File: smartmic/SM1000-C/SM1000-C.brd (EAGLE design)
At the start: 65 x 90 mm, 185 parts, among them CN1 HDR100-3, CN10 MJ-3523-SMT, CN11 HDR100-3, CN12 HRS-DF11-16DS, CN2 MOLEX-MINI-B-SMT, CN3 RASM722PX, CN4 RJ-45, CN5 MJ-3523-SMT, CN6 SJ-3524-SMT, CN7 MJ-3523-SMT, CN8 SJ-3524-SMT, CN9 MJ-3523-SMT, J1 JMP-2PIN, J3 JMP-2PIN, J4 JMP-2PIN, P1 TPAD50, P10 TPAD50, P11 TPAD50, P12 TPAD50, P13 TPAD50, P14 TPAD50, P15 TPAD50, P16 TPAD50, P17 TPAD50, P18 TPAD50, P19 TPAD50, P2 TPAD50, P20 TPAD50, P3 TPAD50, P4 TPAD50, P5 TPAD50, P6 TPAD50, P7 TPAD50, P8 TPAD50, P9 TPAD50, SW1 SW-BOURNS-7914S, SW2 SW-BOURNS-7914S, SW3 DPDT, SW4 SW-BOURNS-7914S, SW5 SW-BOURNS-7914J, T1 SM-LP-5001, T2 SM-LP-5001, U1 STM32F405, U2 LD3985M33R, U3 STMPS2141, U4 EMIF02-USB03F2, U5 TPS54329E, U6 LMV341, U7 LMV341, U8 LM386M-1, U9 LMV341

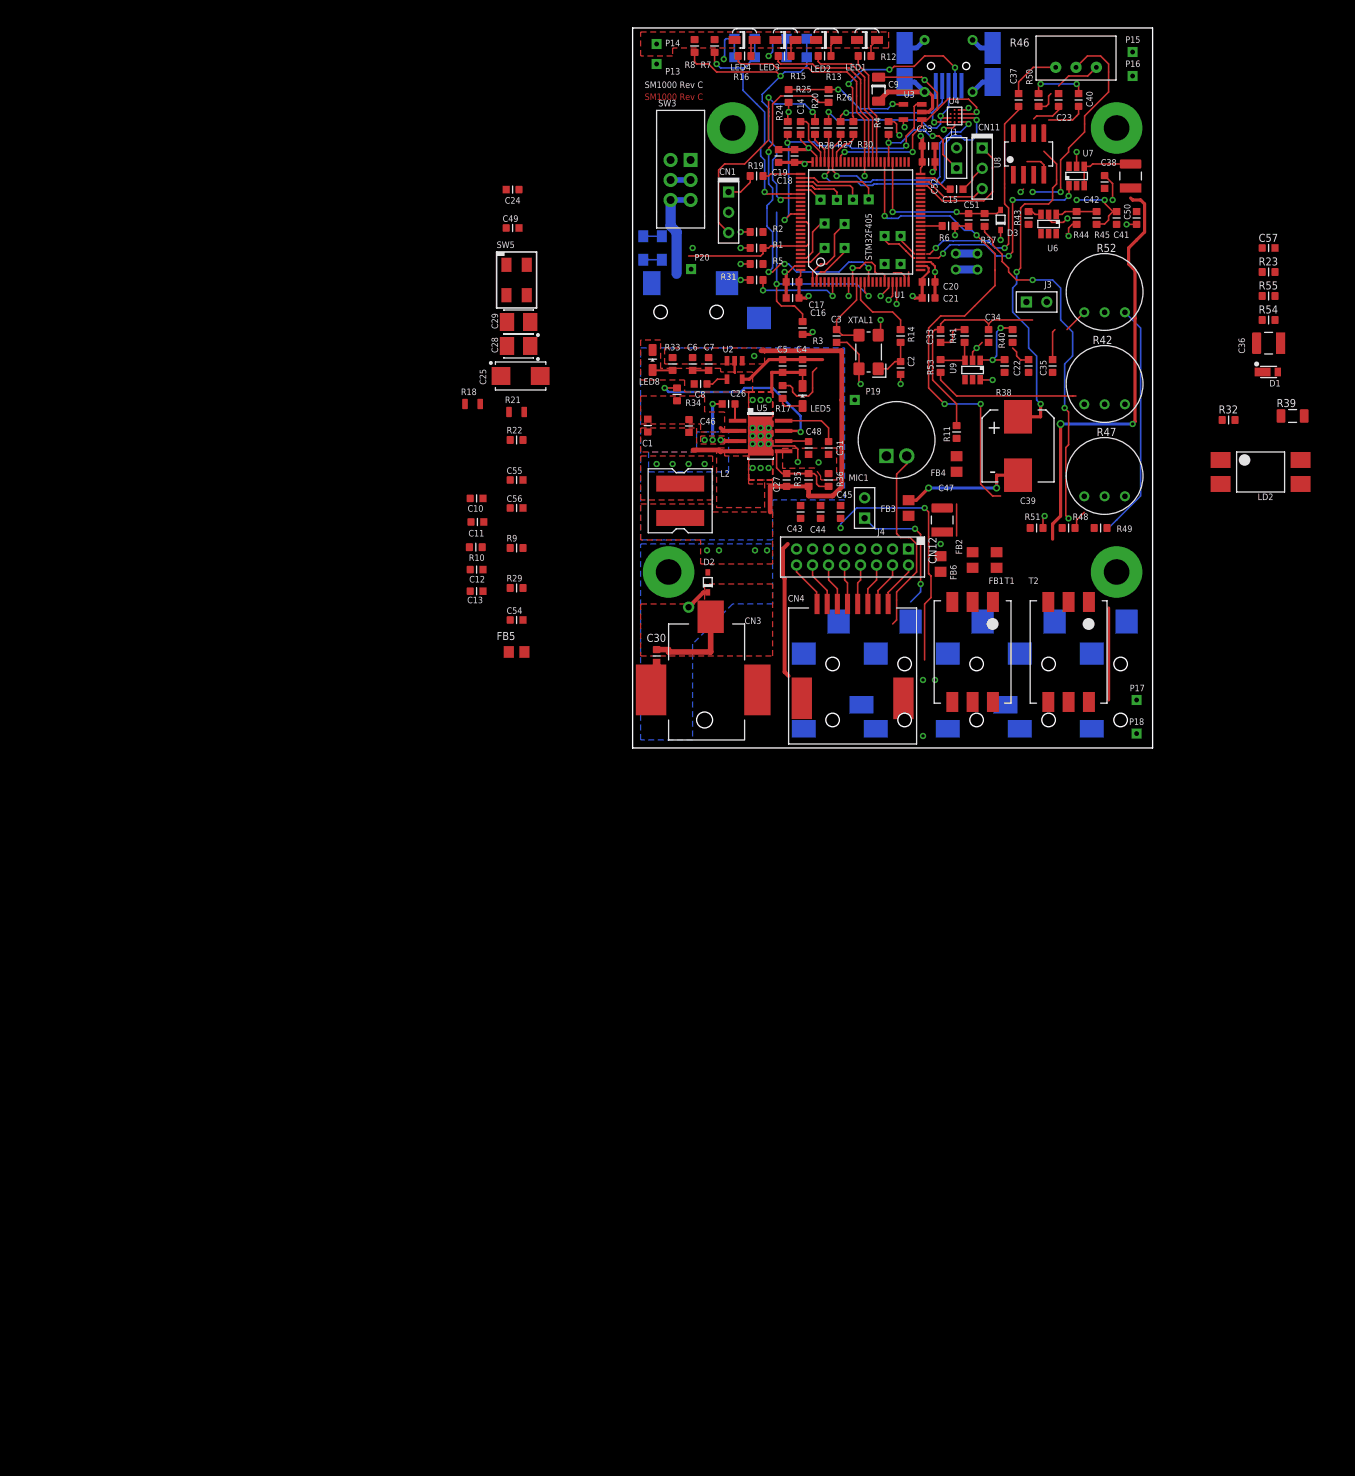
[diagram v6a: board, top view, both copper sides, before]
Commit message: Recovery from Eagle ERC problem RGB
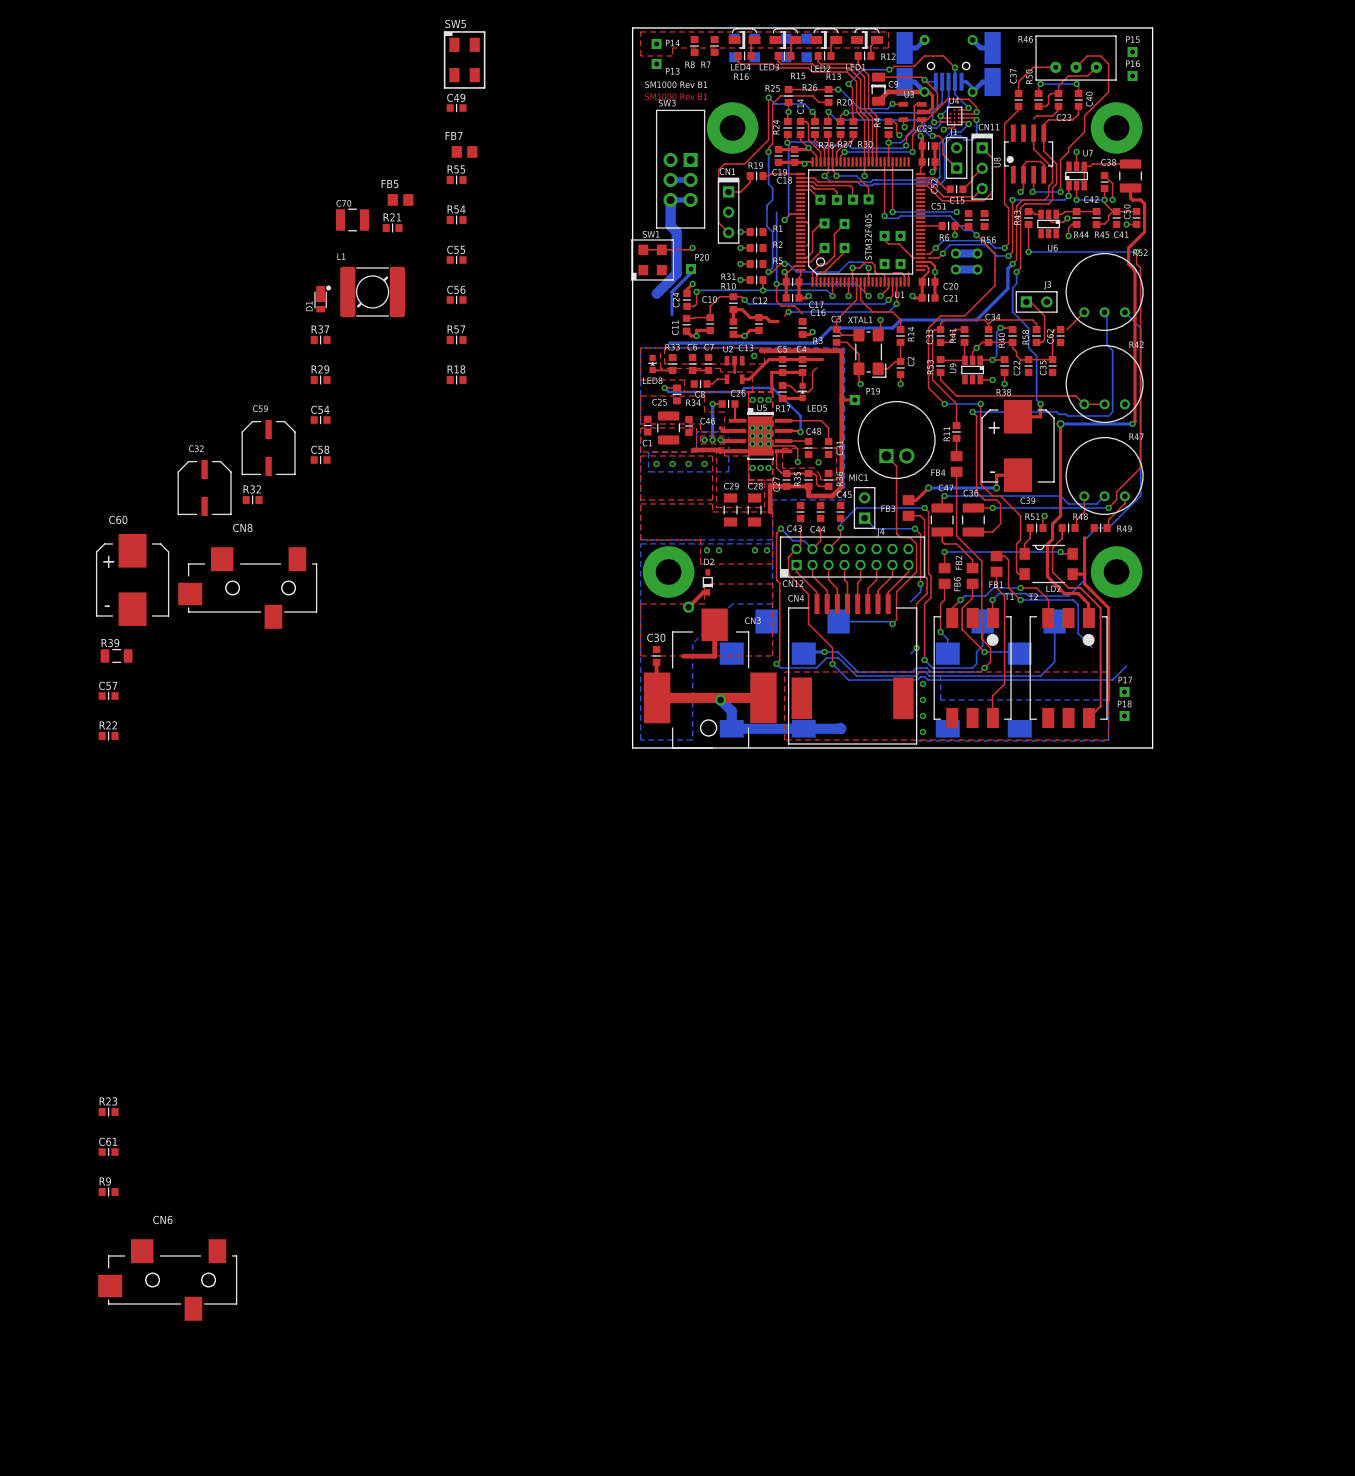
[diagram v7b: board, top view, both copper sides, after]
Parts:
- removed D3: BAT60J, _RoweTel:SOD323R_INFINEON
- removed L2: 4.7uH, _RoweTel:SRN6045
- added C32, C59: 100uF,6.3V,EL, _RoweTel:NICHICON-WX-6.3
- added C58, C61, C62: 100nF,16V, AA-ipc-7351-capacitor:CAPC1608X92N
- added C60: 220uF,25V, _RoweTel:CAP-CHEMI-HA0
- added C70: 22uF,25V,1210, ipc-7351-capacitor:CAPC3225X168N
- added FB7: FB0805, _RoweTel:FE0805
- added L1: 4.2uH, _RoweTel:SRR5028
- added R56, R58: 2.2K,1%, AA-ipc-7351-resistor:RESC1608X55N
- added R57: 470,1%, AA-ipc-7351-resistor:RESC1608X55N
- C25: value 22uF,25V,3528,Tant -> 22uF,25V,1210; device AA-ipc-7351-capacitor:CAPMP6032X280N -> ipc-7351-capacitor:CAPC3225X168N
- C28, C29: value 10uF,25V,3528,Tant -> 10uF,25V,1206; device AA-ipc-7351-capacitor:CAPMP3528X210N -> ipc-7351-capacitor:CAPC3215X168N
- C40: value 47nF,25V -> 100nF,25V
- C54: value 1nF,16V -> 1nF,25V
- CN12: value HRS-DF11-16DS -> DF11-16DS
- CN3: device _RoweTel:RASM722PX -> _RoweTel:RASM712PX
- CN6, CN8: value SJ-3524-SMT -> SJ-3524
- FB5: value (none) -> FB0805
- LD2: device _RoweTel:LTV-817S -> _RoweTel:SMD4
- R18, R21: device _RoweTel:RR0805 -> AA-ipc-7351-resistor:RESC1608X55N
- R32: value (none) -> 100,1%
- R37: value 2.2K,1% -> 10K,1%
- SW1: device SM1000:SW-BOURNS-7914S -> SM1000-2L-70x90:SW-BOURNS-7914S
- moved R23 179.0 mm to (-65.5, -45.5)
- moved C57 155.4 mm to (-65.5, 6.50)
- moved R39 150.0 mm to (-64.5, 11.5)
- moved CN6 123.7 mm to (-56.5, -66.5), flipped to the top, turned to 0 degrees
- moved R32 122.4 mm to (-47.5, 31.0)
- moved D1 119.3 mm to (-39.0, 55.5), turned to 0 degrees
- moved R55 102.5 mm to (-22.0, 71.0)
- moved R54 102.3 mm to (-22.0, 66.0)
- moved R9 95.3 mm to (-65.5, -55.5)
- moved R37 84.3 mm to (-39.0, 51.0), turned to 0 degrees
- moved CN8 72.7 mm to (-46.5, 20.0), flipped to the top, turned to 0 degrees
- moved R22 63.0 mm to (-65.5, 1.50)
- moved FB5 58.3 mm to (-29.0, 68.5)
- moved CN10 47.2 mm to (16.0, 8.00), turned to 270 degrees
- moved C12 46.8 mm to (15.8, 53.0), turned to 270 degrees
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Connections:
- net !CPTT! renamed !CPPT!
- net N$15 renamed +VEXT
- removed net BACK: R8.2, SW4.1, SW4.2, U1.82
- removed net BOOT0: R1.2, SW1.1, SW1.2, U1.88, U1.94
- removed net N$32 (its old number): C54.2, R29.1, R42.1, U9.4
- removed net N$37 (its old number): U8.6
- removed net N$85: CN10.2, R37.1
- removed net S$1: T1.3, T2.3
- removed net S$2: R49.1
- removed net SELECT: R7.2, SW2.1, SW2.2, U1.81
- new net !BACK!: R8.1, SW4.3, SW4.4, U1.82
- new net !BOOT0!: R57.1, U1.88, U1.94
- new net !SELECT!: R7.1, SW2.3, SW2.4, U1.81
- new net APTT: CN12.14, CN9.10
- new net MIC: CN12.15, CN7.10
- new net N$11: R55.1, U1.29
- new net N$14: R1.2, R57.2, SW1.1, SW1.2
- new net N$15: C51.1, CN10.2, R37.2, R56.1
- new net N$26: FB4.2, R11.1
- new net N$27: C54.2, R29.2, R42.3, U9.4
- new net N$33: C44.1, FB1.1, T1.6
- new net N$48: C60.1, R39.2, U8.6
- new net N$64: CN6.2, FB1.2
- new net N$72: CN7.2, FB2.2
- new net N$73: CN9.2, FB6.2
- new net N$76: CN5.2, FB4.1
- new net N$78: R48.2, T2.6
- new net N$81: R47.3, R49.2
- new net RF_MIC: C43.2, CN12.11, CN12.12, CN7.1, R49.1, T2.4
- new net RF_PTT: C45.2, CN12.13, CN9.1, LD2.3
- new net RF_SPKR: C44.2, CN12.10, CN12.9, CN6.1, T1.4
- new net SPKR: CN12.16, CN6.4
- net !EXT-PTT!: now also R56.2; no longer C51.1, D3.A, R37.2
- net +5V: now also C28.1, C29.1, L1.2; no longer C28.+, C29.+, L2.2
- net +VIN: now also C25.1, C70.1, R39.1; no longer C25.+
- net AIN2: no longer P4.1, R29.2
- net AVDD: now also U9.6
- net DAC1_OUT: now also R55.2; no longer R55.1
- net DAC2_OUT: now also R22.1, R54.2; no longer R22.2, R54.1
- net GND: now also C25.2, C28.2, C29.2, C32.2, C58.1, C59.2, C60.2, C61.2, C62.2, C70.2, CN10.1, CN3.1, CN3.3, CN4.10, CN4.9, CN5.1, CN8.1, R22.2, SW2.1, SW2.2, SW4.1, SW4.2, T1.3, T2.3; no longer C25.-, C28.-, C29.-, R22.1, R7.1, R8.1
- net N$13: now also R54.1, U1.30; no longer R47.1, R49.2
- net N$24: now also FB5.2
- net N$25: now also R58.1
- net N$29: now also J3.1, R32.2; no longer R55.2, U1.29
- net N$36: now also P4.1, R29.1; no longer R54.2, U1.30
- net N$41: now also R42.1; no longer R42.3
- net N$45: now also C32.1, C62.1, R32.1, R58.2; no longer J3.1
- net N$46: now also C58.2, C59.1
- net N$5: now also FB7.2
- net N$51: now also CN12.8; no longer CN12.16
- net N$52: now also CN12.7; no longer CN12.15
- net N$53: now also CN12.6; no longer CN12.14
- net N$54: now also CN12.5; no longer CN12.13
- net N$55: now also CN12.4; no longer CN12.12
- net N$56: now also CN12.3; no longer CN12.11
- net N$57: now also CN12.2; no longer CN12.10
- net N$58: now also CN12.1; no longer CN12.9
- net N$59: now also C61.1
- net N$60: now also CN5.10
- net N$62: now also CN8.4
- net N$74: now also C45.1
- net N$75: now also CN8.2, CN8.3
- net N$77: now also FB5.1
- net N$82: now also R47.1; no longer R47.3
- net SW: now also L1.1; no longer L2.1
- net VDD: now also FB7.1, R37.1, R7.2, R8.2; no longer D3.C, SW2.3, SW2.4, SW4.3, SW4.4, U9.6
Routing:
- net GND: track 146.7 -> 228.0 mm, vias 40 -> 46
- net VDD: track 122.0 -> 51.9 mm, vias 19 -> 15
- net N$48: track 0.00 -> 69.4 mm, vias 0 -> 1
- net MIC: track 0.00 -> 68.1 mm, vias 0 -> 2
- net N$50: track 0.00 -> 67.7 mm, vias 0 -> 4
- net SPKR: track 0.00 -> 58.6 mm, vias 0 -> 1
- net N$9: track 0.00 -> 50.9 mm, vias 0 -> 1
- net N$76: track 4.00 -> 50.9 mm, vias 0 -> 2
- net N$85: track 44.6 -> 0.00 mm, vias 3 -> 0
- net BACK: track 40.4 -> 0.00 mm, vias 2 -> 0
- net SELECT: track 31.2 -> 0.00 mm, vias 2 -> 0
- net N$78: track 0.00 -> 28.2 mm
- net N$4: track 2.46 -> 30.2 mm, vias 1 -> 2
- net N$63: track 29.4 -> 53.1 mm, vias 0 -> 1
- net RF_PTT: track 0.00 -> 23.0 mm
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- added copper zone on layer 1, net RF
- added copper zone on layer 16, net RF
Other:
- board text added: "SM1000 Rev B1"
- board text removed: "SM1000 Rev C"

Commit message: Update SM1000-C schematics RGB
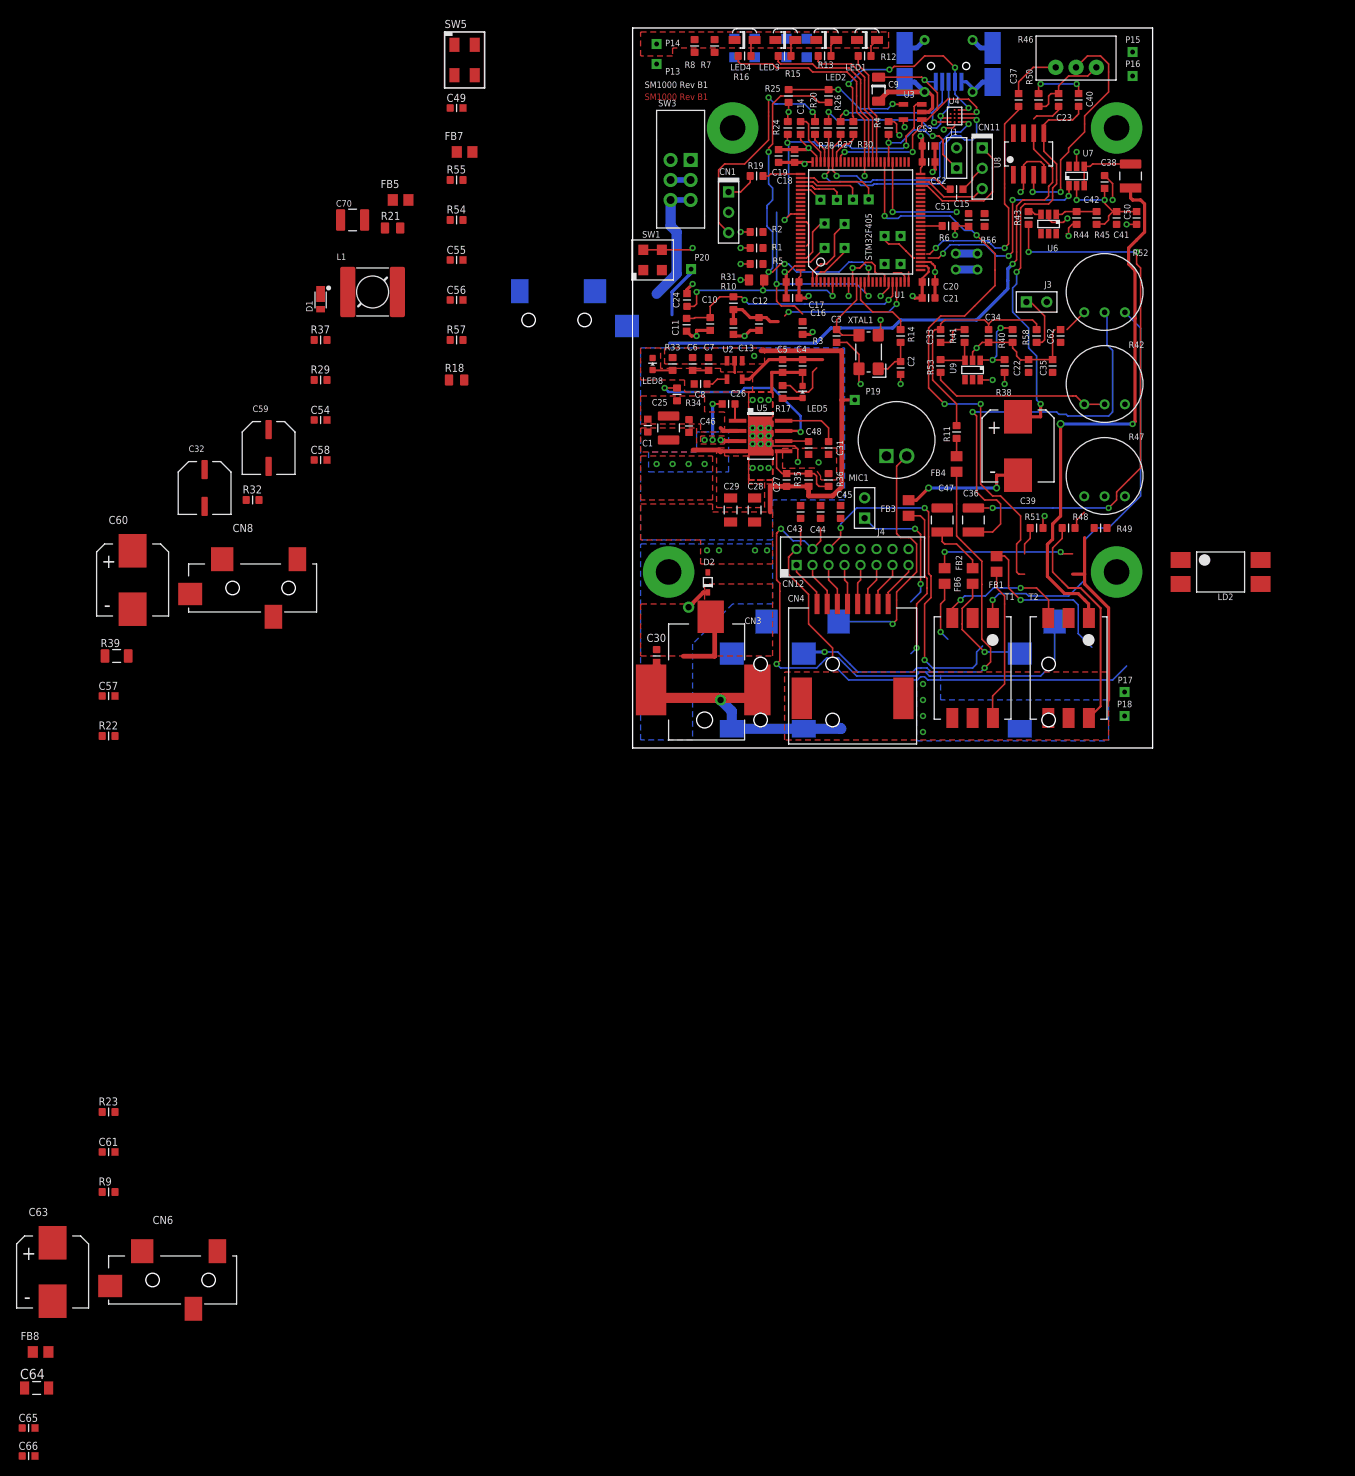
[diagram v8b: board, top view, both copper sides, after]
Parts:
- added C63: 220uF,25V, _RoweTel:CAP-CHEMI-HA0
- added C64: 10uF,25V,1206, ipc-7351-capacitor:CAPC3215X168N
- added C65: 1uF,16V, AA-ipc-7351-capacitor:CAPC1608X92N
- added C66: 100nF,16V, AA-ipc-7351-capacitor:CAPC1608X92N
- added FB8: FB0805, _RoweTel:FE0805
- C40: value 100nF,25V -> 47nF,25V
- C54: value 1nF,25V -> 100pF,25V
- CN3: device _RoweTel:RASM712PX -> _RoweTel:RASM722PX
- LD2: device _RoweTel:SMD4 -> _RoweTel:LTV-817S
- R18, R21, R31: device AA-ipc-7351-resistor:RESC1608X55N -> AA-ipc-7351-resistor:RESC2012X70N
- R23: value 10K,1% -> 47K,1%
- moved CN9 68.7 mm to (-8.50, 53.5), turned to 0 degrees
- moved LD2 21.5 mm to (73.5, 22.0)
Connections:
- net +VEXT renamed N$81
- removed net N$36: P4.1, R29.1
- removed net N$81 (its old number): R47.3, R49.2
- new net N$61: R47.1, R49.2
- net AIN2: now also P4.1, R29.1
- net AVDD: now also C64.1, C65.1, C66.1, FB8.2
- net GND: now also C63.2, C64.2, C65.2, C66.2
- net N$70: now also C63.1
- net N$82: now also R47.3; no longer R47.1
- net VDD: now also FB8.1
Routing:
- net N$80: track 22.4 -> 0.00 mm, vias 1 -> 0
- net N$81 (its old number): track 4.89 -> 0.00 mm
- net APTT: track 47.5 -> 44.4 mm
- net N$82: track 4.44 -> 2.44 mm
- net N$73: track 9.30 -> 7.50 mm
